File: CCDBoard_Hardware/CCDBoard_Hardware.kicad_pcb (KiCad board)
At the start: 2 copper layers, 3 parts, among them U1 TCD1304

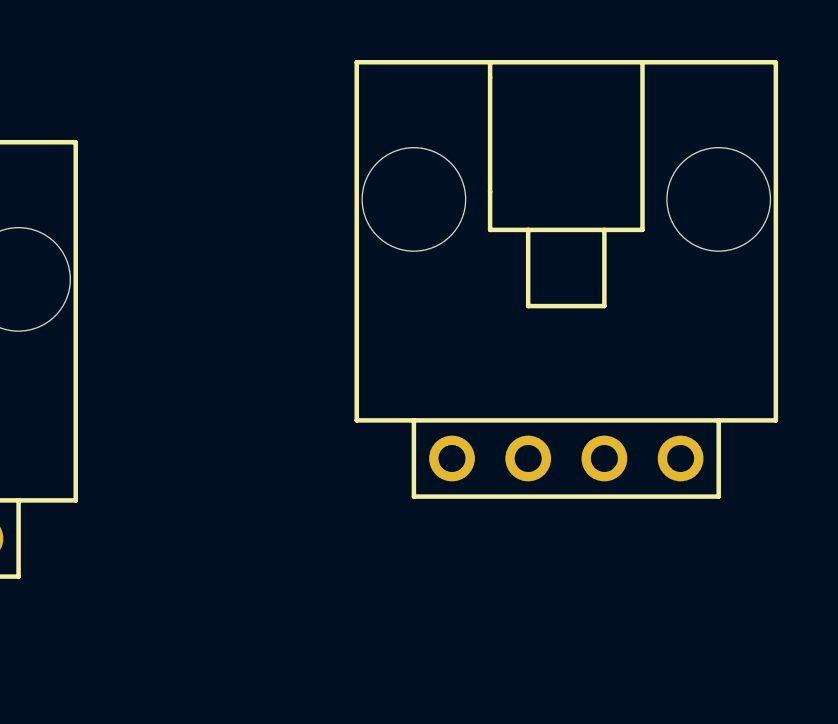
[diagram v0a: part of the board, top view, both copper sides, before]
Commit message: updates Sensorboard connector
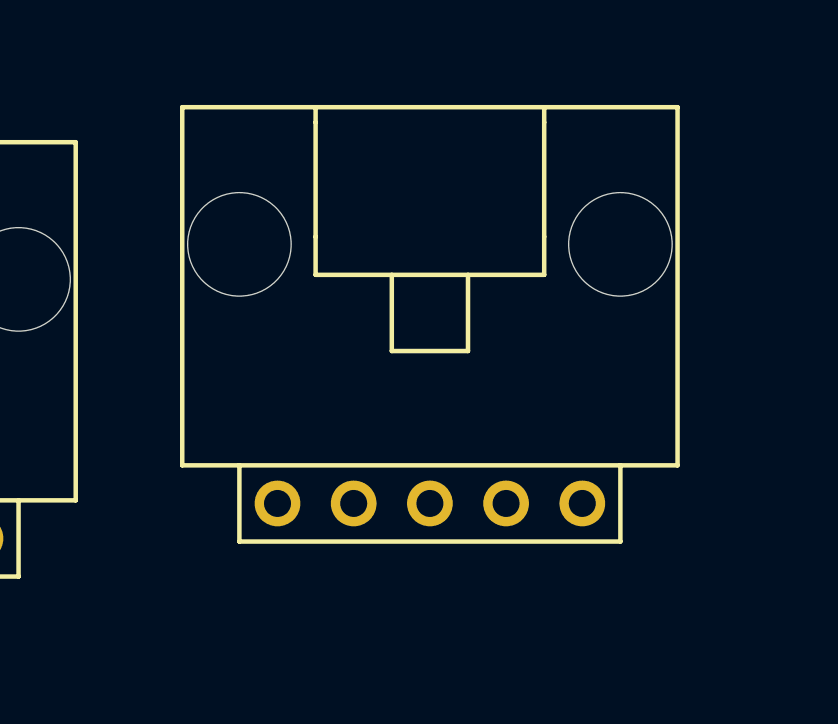
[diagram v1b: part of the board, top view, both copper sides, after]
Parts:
- Conn1: value Molex_SL_04 -> Molex_SL_05; footprint MRDT_Connectors:MOLEX_SL_04_Horizontal -> MRDT_Connectors:MOLEX_SL_05_Horizontal
- moved Conn1 4.79 mm to (175.9, 61.3)
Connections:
- Conn1 pad 1: Sync2 -> +3V3
- Conn1 pad 2: Sync1 -> Sync2
- Conn1 pad 3: OS -> Sync1
- Conn1 pad 4: GND -> OS
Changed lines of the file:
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@@
     (solder_mask_min_width 0.25)
     (aux_axis_origin 0 0)
-    (visible_elements FFFFFF7F)
+    (visible_elements 7FFFFFFF)
     (pcbplotparams
       (layerselection 0x010fc_ffffffff)
@@
       (net 7 GND))
   )
-  (module MRDT_Connectors:MOLEX_SL_04_Horizontal (layer F.Cu)
-    (at 180.4416 59.817)
-    (fp_text reference Conn1 (at -2.54 2.54) (layer F.SilkS) hide
+  (module MRDT_Connectors:MOLEX_SL_05_Horizontal (layer F.Cu)
+    (at 175.895 61.3156)
+    (fp_text reference Conn1 (at -3.81 2.54) (layer F.SilkS) hide
       (effects (font (size 1 1) (thickness 0.15)))
     )
-    (fp_text value Molex_SL_04 (at -0.635 2.032) (layer F.Fab)
+    (fp_text value Molex_SL_05 (at 0 2.54) (layer F.Fab)
       (effects (font (size 1 1) (thickness 0.15)))
     )
-    (fp_line (start -6.985 -13.208) (end 6.985 -13.208) (layer F.SilkS) (width 0.15))
-    (fp_line (start -2.54 -7.62) (end 2.54 -7.62) (layer F.SilkS) (width 0.15))
-    (fp_line (start 1.27 -7.62) (end 1.27 -5.08) (layer F.SilkS) (width 0.15))
-    (fp_line (start 1.27 -5.08) (end -1.27 -5.08) (layer F.SilkS) (width 0.15))
-    (fp_line (start 2.54 -13.208) (end 2.54 -7.62) (layer F.SilkS) (width 0.15))
-    (fp_line (start 6.985 -1.27) (end 6.985 -13.208) (layer F.SilkS) (width 0.15))
-    (fp_line (start 5.08 1.27) (end -5.08 1.27) (layer F.SilkS) (width 0.15))
-    (fp_line (start -2.54 -13.208) (end -2.54 -12.7) (layer F.SilkS) (width 0.15))
-    (fp_line (start -6.985 -1.27) (end -6.985 -13.208) (layer F.SilkS) (width 0.15))
-    (fp_line (start -5.08 -1.27) (end -6.985 -1.27) (layer F.SilkS) (width 0.15))
-    (fp_line (start -2.54 -8.89) (end -2.54 -7.62) (layer F.SilkS) (width 0.15))
-    (fp_line (start -2.54 -8.89) (end -2.54 -12.7) (layer F.SilkS) (width 0.15))
+    (fp_line (start -3.81 -13.208) (end -3.81 -12.7) (layer F.SilkS) (width 0.15))
+    (fp_line (start 3.81 -12.7) (end 3.81 -13.208) (layer F.SilkS) (width 0.15))
+    (fp_line (start -8.255 -13.208) (end 8.255 -13.208) (layer F.SilkS) (width 0.15))
+    (fp_line (start -8.255 -1.27) (end -8.255 -13.208) (layer F.SilkS) (width 0.15))
+    (fp_line (start 8.255 -1.27) (end 8.255 -13.208) (layer F.SilkS) (width 0.15))
+    (fp_line (start 6.35 -1.27) (end 8.255 -1.27) (layer F.SilkS) (width 0.15))
+    (fp_line (start -6.35 -1.27) (end -8.255 -1.27) (layer F.SilkS) (width 0.15))
+    (fp_line (start -3.81 -8.89) (end -3.81 -7.62) (layer F.SilkS) (width 0.15))
+    (fp_line (start -3.81 -7.62) (end 3.81 -7.62) (layer F.SilkS) (width 0.15))
+    (fp_line (start 3.81 -7.62) (end 3.81 -8.89) (layer F.SilkS) (width 0.15))
+    (fp_line (start 3.81 -8.89) (end 3.81 -12.7) (layer F.SilkS) (width 0.15))
+    (fp_line (start -3.81 -8.89) (end -3.81 -12.7) (layer F.SilkS) (width 0.15))
     (fp_line (start -1.27 -7.62) (end -1.27 -5.08) (layer F.SilkS) (width 0.15))
-    (fp_line (start -5.08 -1.27) (end 6.985 -1.27) (layer F.SilkS) (width 0.15))
-    (fp_line (start 5.08 -1.27) (end 5.08 1.27) (layer F.SilkS) (width 0.15))
-    (fp_line (start -5.08 1.27) (end -5.08 -1.27) (layer F.SilkS) (width 0.15))
-    (pad 1 thru_hole circle (at -3.81 0) (size 1.524 1.524) (drill 0.9) (layers *.Cu *.Mask)
+    (fp_line (start -1.27 -5.08) (end 1.27 -5.08) (layer F.SilkS) (width 0.15))
+    (fp_line (start 1.27 -5.08) (end 1.27 -7.62) (layer F.SilkS) (width 0.15))
+    (fp_line (start -6.35 -1.27) (end 6.35 -1.27) (layer F.SilkS) (width 0.15))
+    (fp_line (start 6.35 -1.27) (end 6.35 1.27) (layer F.SilkS) (width 0.15))
+    (fp_line (start 6.35 1.27) (end -6.35 1.27) (layer F.SilkS) (width 0.15))
+    (fp_line (start -6.35 1.27) (end -6.35 -1.27) (layer F.SilkS) (width 0.15))
+    (pad 1 thru_hole circle (at -5.08 0) (size 1.524 1.524) (drill 0.9) (layers *.Cu *.Mask)
+      (net 3 +3V3))
+    (pad 2 thru_hole circle (at -2.54 0) (size 1.524 1.524) (drill 0.9) (layers *.Cu *.Mask)
       (net 1 Sync2))
-    (pad 2 thru_hole circle (at -1.27 0) (size 1.524 1.524) (drill 0.9) (layers *.Cu *.Mask)
+    (pad 3 thru_hole circle (at 0 0) (size 1.524 1.524) (drill 0.9) (layers *.Cu *.Mask)
       (net 2 Sync1))
-    (pad 3 thru_hole circle (at 1.27 0) (size 1.524 1.524) (drill 0.9) (layers *.Cu *.Mask)
+    (pad 4 thru_hole circle (at 2.54 0) (size 1.524 1.524) (drill 0.9) (layers *.Cu *.Mask)
       (net 8 OS))
-    (pad 4 thru_hole circle (at 3.81 0) (size 1.524 1.524) (drill 0.9) (layers *.Cu *.Mask)
+    (pad 5 thru_hole circle (at 5.08 0) (size 1.524 1.524) (drill 0.9) (layers *.Cu *.Mask)
       (net 7 GND))
-    (pad "" np_thru_hole circle (at -5.08 -8.636) (size 3.45 3.45) (drill 3.45) (layers *.Cu *.Mask))
-    (pad "" np_thru_hole circle (at 5.08 -8.636) (size 3.45 3.45) (drill 3.45) (layers *.Cu *.Mask))
-    (model "${MRDT_KICAD_LIBRARIES}/3D Files/MRDT_Connctors/Molex_SL_04_Horizontal.stp"
-      (offset (xyz 6.349999904632568 12.95399980545044 0))
+    (pad "" np_thru_hole circle (at -6.35 -8.636) (size 3.45 3.45) (drill 3.45) (layers *.Cu *.Mask))
+    (pad "" np_thru_hole circle (at 6.35 -8.636) (size 3.45 3.45) (drill 3.45) (layers *.Cu *.Mask))
+    (model "${MRDT_KICAD_LIBRARIES}/3D Files/MRDT_Connctors/Molex_SL_05_Horizontal.stp"
+      (offset (xyz 7.619999885559082 12.95399980545044 0))
       (scale (xyz 1 1 1))
       (rotate (xyz 0 0 180))

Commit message: Layout and step
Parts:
- added REF**: 4_40_Hole, MRDT_Drill_Holes:4_40_Hole, F.Cu at (48.3, -12.7)
- added REF**: 4_40_Hole, MRDT_Drill_Holes:4_40_Hole, F.Cu at (48.3, -2.54)
- added REF**: 4_40_Hole, MRDT_Drill_Holes:4_40_Hole, F.Cu at (2.54, -12.7)
- added REF**: 4_40_Hole, MRDT_Drill_Holes:4_40_Hole, F.Cu at (2.54, -2.54)
- Conn1: footprint MRDT_Connectors:MOLEX_SL_05_Horizontal -> MRDT_Connectors:MOLEX_SL_05_Vertical
- Conn2: footprint MRDT_Connectors:MOLEX_SL_07_Horizontal -> MRDT_Connectors:MOLEX_SL_07_Vertical
- U1: moved to B.Cu
- moved Conn1 158.9 mm to (38.1, -17.8)
- moved Conn2 157.5 mm to (17.8, -17.8)
- moved U1 141.6 mm to (4.60, -12.4), turned to 270 degrees
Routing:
- net OS: track 0.00 -> 39.0 mm
- net +3V3: track 0.00 -> 33.8 mm
- net Sync1: track 0.00 -> 24.8 mm
- net Sync2: track 0.00 -> 24.1 mm
- net SH: track 0.00 -> 10.8 mm
- net M: track 0.00 -> 6.13 mm
- net ICG: track 0.00 -> 5.08 mm
- added copper zone on B.Cu, net GND
- added copper zone on F.Cu, net GND
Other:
- board outline added: 50.8 x 21.1 mm
- board text added: "3V3"
- board text added: "GND"
- board text added: "ICG"
- board text added: "M"
- board text added: "OS"
- board text added: "S1"
- board text added: "S2"
- board text added: "SH"
